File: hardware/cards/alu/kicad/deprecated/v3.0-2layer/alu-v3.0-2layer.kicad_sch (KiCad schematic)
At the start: 0 parts

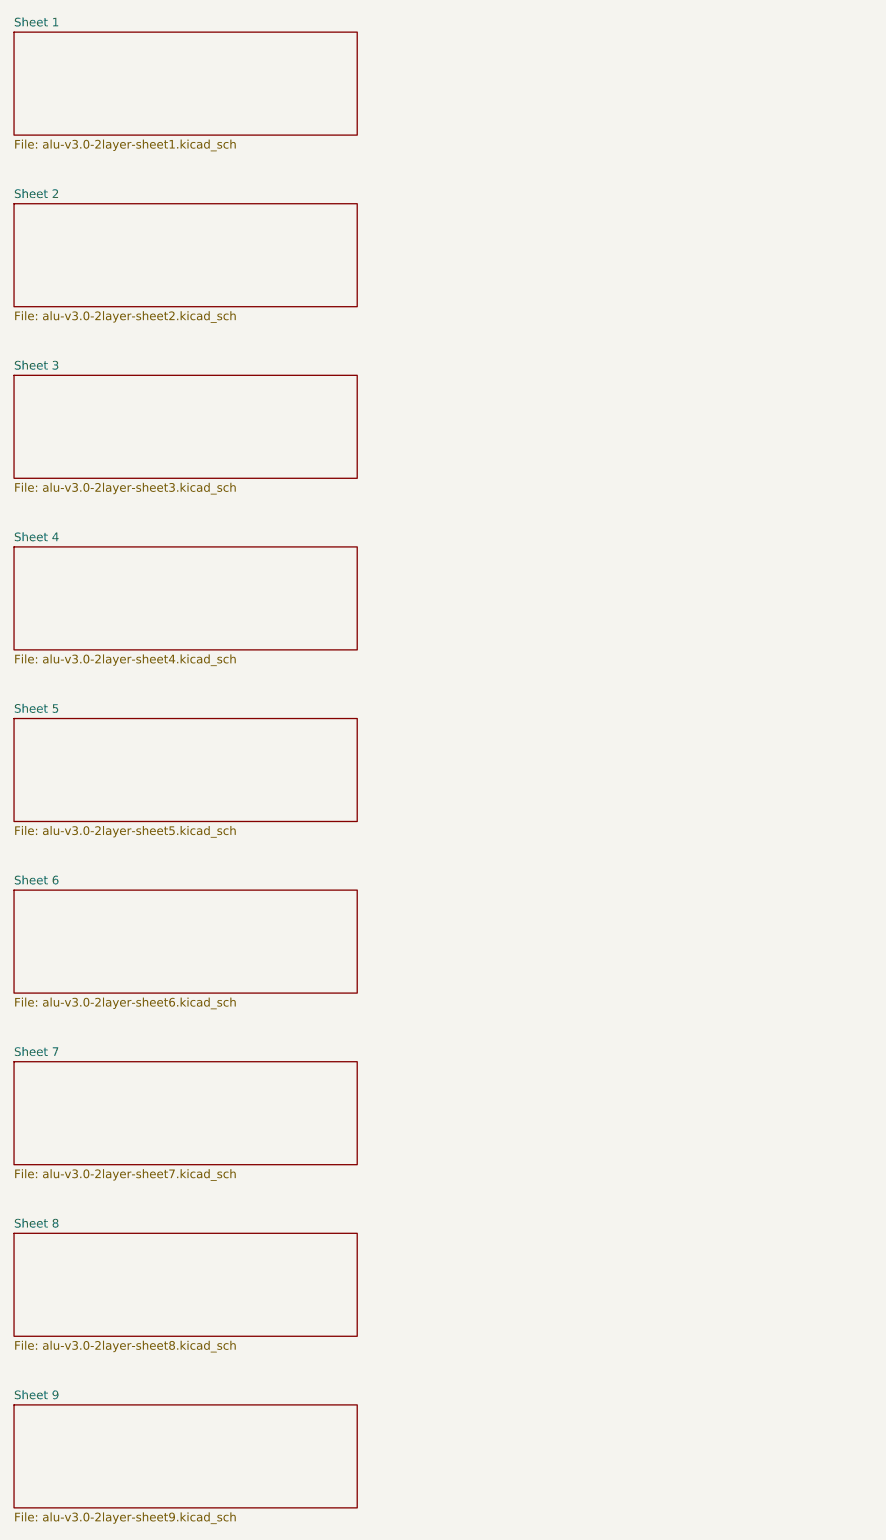
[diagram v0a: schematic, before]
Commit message: fix(kicad): readable converted schematics - overlaps 42,847 -> 3,147, nothing off the frame; CF sheet 0 overlaps
- tools/kicad/sch_overlaps.py: calibrated readability check (text/text, text/body, text/line, off frame/title block)
- eagle_sch_to_kicad.py: fields placed from Eagle's smashed attributes or the symbol's >NAME/>VALUE with Eagle's align,
  size and ratio, readable angles; fields Eagle never shows hidden (FABC96R shows only its pin name); pin numbers hidden
  where every Eagle pin hides them; Eagle-hidden layers dropped (the stray SpiceOrder text); labels on their own wires,
  converter labels only where KiCad needs them; rotate-then-mirror fixed for MR90/MR270 in pin_world/no-connects;
  each sheet on the smallest page that holds it, centred clear of the title block
- finish_board.py: stable footprint-library choice (DRC counts no longer vary run to run)
- all 37 projects regenerated: netlist proofs unchanged (34 MATCH, 2 schematic-only, video Fusion export MISMATCH as
  before); DRC same or better; ERC up (loose wire ends onto graphic buses no longer hidden by labels; explained per README)
- CF card: gate names off the gate bodies, U3 clear of its title, 5.08 mm connector pins; rebuilt: DRC 0/0, proof MATCH
- schematic PDFs regenerated (tools/sch_to_pdf.py, 37/37)

Co-Authored-By: Claude Opus 5.5 <noreply@anthropic.com>
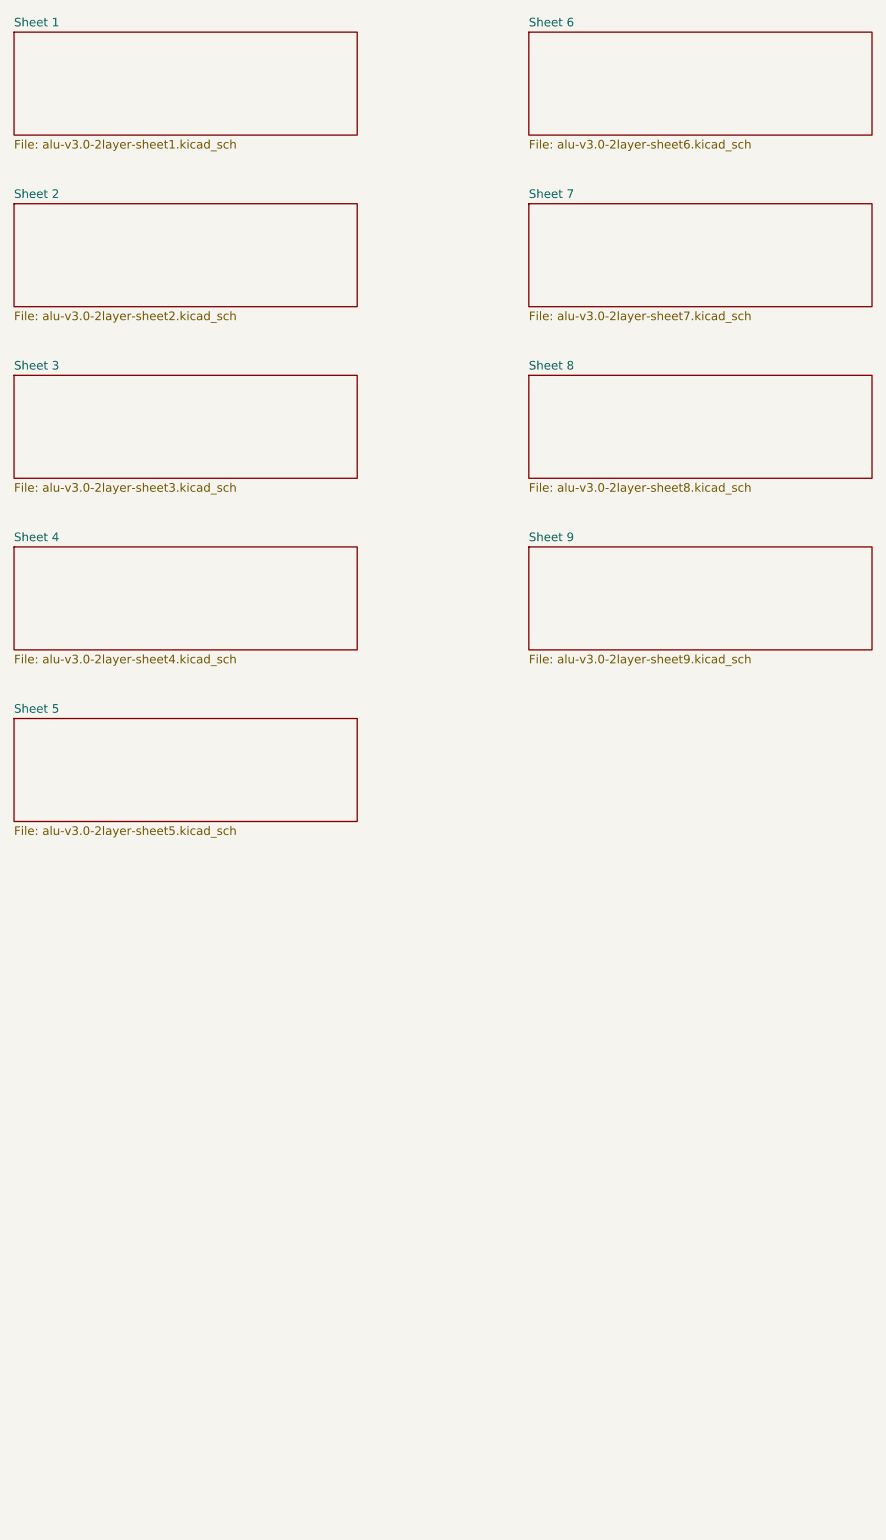
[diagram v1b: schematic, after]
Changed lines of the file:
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@@
 		(instances (project "alu-v3.0-2layer" (path "/ce2c65fa-7716-eccf-9f71-4bde28d62d35" (page "6"))))
 	)
-	(sheet (at 25.4 152.4) (size 50.8 15.24) (exclude_from_sim no) (in_bom yes) (on_board yes) (dnp no) (fields_autoplaced yes)
+	(sheet (at 101.6 25.4) (size 50.8 15.24) (exclude_from_sim no) (in_bom yes) (on_board yes) (dnp no) (fields_autoplaced yes)
 		(stroke (width 0.1524) (type solid)) (fill (color 0 0 0 0.0))
-		(property "Sheetname" "Sheet 6" (at 25.4 151.7 0) (effects (font (size 1.27 1.27)) (justify left bottom)))
-		(property "Sheetfile" "alu-v3.0-2layer-sheet6.kicad_sch" (at 25.4 168.3 0) (effects (font (size 1.27 1.27)) (justify left top)))
+		(property "Sheetname" "Sheet 6" (at 101.6 24.7 0) (effects (font (size 1.27 1.27)) (justify left bottom)))
+		(property "Sheetfile" "alu-v3.0-2layer-sheet6.kicad_sch" (at 101.6 41.3 0) (effects (font (size 1.27 1.27)) (justify left top)))
 		(instances (project "alu-v3.0-2layer" (path "/ce2c65fa-7716-eccf-9f71-4bde28d62d35" (page "7"))))
 	)
-	(sheet (at 25.4 177.8) (size 50.8 15.24) (exclude_from_sim no) (in_bom yes) (on_board yes) (dnp no) (fields_autoplaced yes)
+	(sheet (at 101.6 50.8) (size 50.8 15.24) (exclude_from_sim no) (in_bom yes) (on_board yes) (dnp no) (fields_autoplaced yes)
 		(stroke (width 0.1524) (type solid)) (fill (color 0 0 0 0.0))
-		(property "Sheetname" "Sheet 7" (at 25.4 177.1 0) (effects (font (size 1.27 1.27)) (justify left bottom)))
-		(property "Sheetfile" "alu-v3.0-2layer-sheet7.kicad_sch" (at 25.4 193.7 0) (effects (font (size 1.27 1.27)) (justify left top)))
+		(property "Sheetname" "Sheet 7" (at 101.6 50.1 0) (effects (font (size 1.27 1.27)) (justify left bottom)))
+		(property "Sheetfile" "alu-v3.0-2layer-sheet7.kicad_sch" (at 101.6 66.7 0) (effects (font (size 1.27 1.27)) (justify left top)))
 		(instances (project "alu-v3.0-2layer" (path "/ce2c65fa-7716-eccf-9f71-4bde28d62d35" (page "8"))))
 	)
-	(sheet (at 25.4 203.2) (size 50.8 15.24) (exclude_from_sim no) (in_bom yes) (on_board yes) (dnp no) (fields_autoplaced yes)
+	(sheet (at 101.6 76.2) (size 50.8 15.24) (exclude_from_sim no) (in_bom yes) (on_board yes) (dnp no) (fields_autoplaced yes)
 		(stroke (width 0.1524) (type solid)) (fill (color 0 0 0 0.0))
-		(property "Sheetname" "Sheet 8" (at 25.4 202.5 0) (effects (font (size 1.27 1.27)) (justify left bottom)))
-		(property "Sheetfile" "alu-v3.0-2layer-sheet8.kicad_sch" (at 25.4 219.1 0) (effects (font (size 1.27 1.27)) (justify left top)))
+		(property "Sheetname" "Sheet 8" (at 101.6 75.5 0) (effects (font (size 1.27 1.27)) (justify left bottom)))
+		(property "Sheetfile" "alu-v3.0-2layer-sheet8.kicad_sch" (at 101.6 92.1 0) (effects (font (size 1.27 1.27)) (justify left top)))
 		(instances (project "alu-v3.0-2layer" (path "/ce2c65fa-7716-eccf-9f71-4bde28d62d35" (page "9"))))
 	)
-	(sheet (at 25.4 228.6) (size 50.8 15.24) (exclude_from_sim no) (in_bom yes) (on_board yes) (dnp no) (fields_autoplaced yes)
+	(sheet (at 101.6 101.6) (size 50.8 15.24) (exclude_from_sim no) (in_bom yes) (on_board yes) (dnp no) (fields_autoplaced yes)
 		(stroke (width 0.1524) (type solid)) (fill (color 0 0 0 0.0))
-		(property "Sheetname" "Sheet 9" (at 25.4 227.9 0) (effects (font (size 1.27 1.27)) (justify left bottom)))
-		(property "Sheetfile" "alu-v3.0-2layer-sheet9.kicad_sch" (at 25.4 244.5 0) (effects (font (size 1.27 1.27)) (justify left top)))
+		(property "Sheetname" "Sheet 9" (at 101.6 100.9 0) (effects (font (size 1.27 1.27)) (justify left bottom)))
+		(property "Sheetfile" "alu-v3.0-2layer-sheet9.kicad_sch" (at 101.6 117.5 0) (effects (font (size 1.27 1.27)) (justify left top)))
 		(instances (project "alu-v3.0-2layer" (path "/ce2c65fa-7716-eccf-9f71-4bde28d62d35" (page "10"))))
 	)
